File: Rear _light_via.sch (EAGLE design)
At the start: 9 parts

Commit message: via gerbers generated
via boards completed and gerbers generated
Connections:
- net N$4 renamed BRAKE_L
- net N$5 renamed DRIVE_R
- net N$6 renamed BRAKE_R
- net N$8 renamed DRIVE_L
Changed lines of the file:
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@@
 <?xml version="1.0" encoding="utf-8"?>
 <!DOCTYPE eagle SYSTEM "eagle.dtd">
-<eagle version="8.3.1">
+<eagle version="8.6.0">
 <drawing>
 <settings>
@@
 <wire x1="63.5" y1="27.94" x2="114.3" y2="27.94" width="0.1524" layer="91"/>
 <pinref part="L_DRIVE" gate="G$1" pin="V/SIG"/>
-</segment>
-</net>
-<net name="N$4" class="0">
+<label x="71.12" y="27.94" size="1.778" layer="95"/>
+</segment>
+</net>
+<net name="BRAKE_L" class="0">
 <segment>
 <pinref part="REAR" gate="G$1" pin="4"/>
@@
 <wire x1="101.6" y1="53.34" x2="102.87" y2="53.34" width="0.1524" layer="91"/>
 <wire x1="102.87" y1="53.34" x2="114.3" y2="53.34" width="0.1524" layer="91"/>
-</segment>
-</net>
-<net name="N$6" class="0">
+<label x="78.74" y="53.34" size="1.778" layer="95"/>
+</segment>
+</net>
+<net name="BRAKE_R" class="0">
 <segment>
 <pinref part="REAR" gate="G$1" pin="6"/>
@@
 <wire x1="101.6" y1="71.12" x2="102.87" y2="71.12" width="0.1524" layer="91"/>
 <wire x1="102.87" y1="71.12" x2="114.3" y2="71.12" width="0.1524" layer="91"/>
-</segment>
-</net>
-<net name="N$8" class="0">
+<label x="73.66" y="66.04" size="1.778" layer="95"/>
+</segment>
+</net>
+<net name="DRIVE_L" class="0">
 <segment>
 <pinref part="REAR" gate="G$1" pin="8"/>
@@
 <wire x1="86.36" y1="71.12" x2="86.36" y2="91.44" width="0.1524" layer="91"/>
 <wire x1="86.36" y1="91.44" x2="111.76" y2="91.44" width="0.1524" layer="91"/>
+<label x="73.66" y="71.12" size="1.778" layer="95"/>
 </segment>
 </net>
@@
 <pinref part="L_SIG" gate="G$1" pin="V/SIG"/>
 <wire x1="71.12" y1="48.26" x2="114.3" y2="48.26" width="0.1524" layer="91"/>
+<label x="76.2" y="48.26" size="1.778" layer="95"/>
 </segment>
 </net>
@@
 <pinref part="R_SIG" gate="G$1" pin="V/SIG"/>
 <wire x1="106.68" y1="66.04" x2="114.3" y2="66.04" width="0.1524" layer="91"/>
-</segment>
-</net>
-<net name="N$5" class="0">
+<label x="81.28" y="63.5" size="1.778" layer="95"/>
+</segment>
+</net>
+<net name="DRIVE_R" class="0">
 <segment>
 <pinref part="REAR" gate="G$1" pin="7"/>
@@
 <pinref part="L_DRIVE" gate="G$1" pin="G/LOW"/>
 <wire x1="58.42" y1="33.02" x2="114.3" y2="33.02" width="0.1524" layer="91"/>
+<label x="71.12" y="33.02" size="1.778" layer="95"/>
 </segment>
 </net>
@@
 <pinref part="T_DRIVE" gate="G$1" pin="V/SIG"/>
 <wire x1="66.04" y1="86.36" x2="111.76" y2="86.36" width="0.1524" layer="91"/>
-</segment>
-</net>
+<label x="71.12" y="86.36" size="1.778" layer="95"/>
+</segment>
+</net>

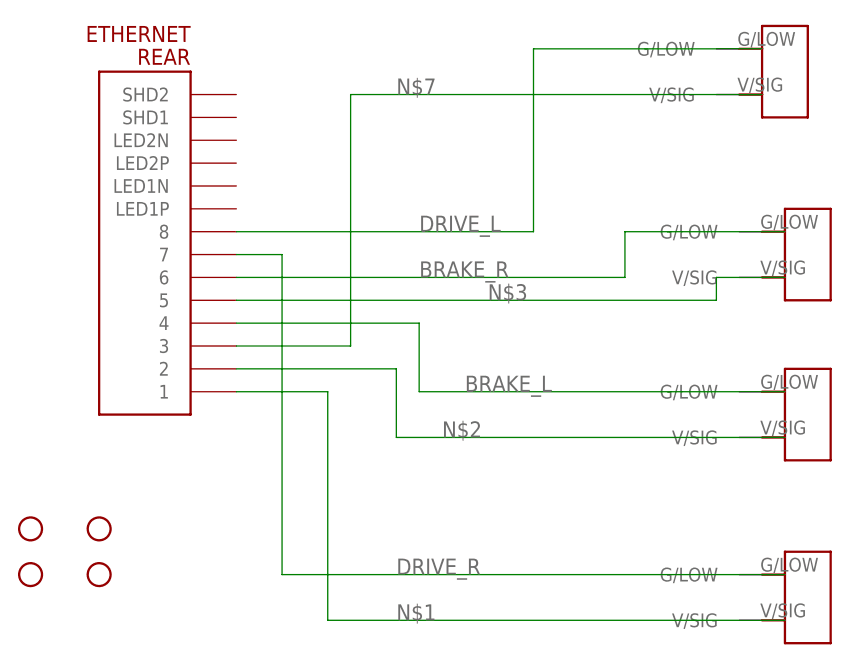
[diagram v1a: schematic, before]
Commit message: added reverse polairity protection
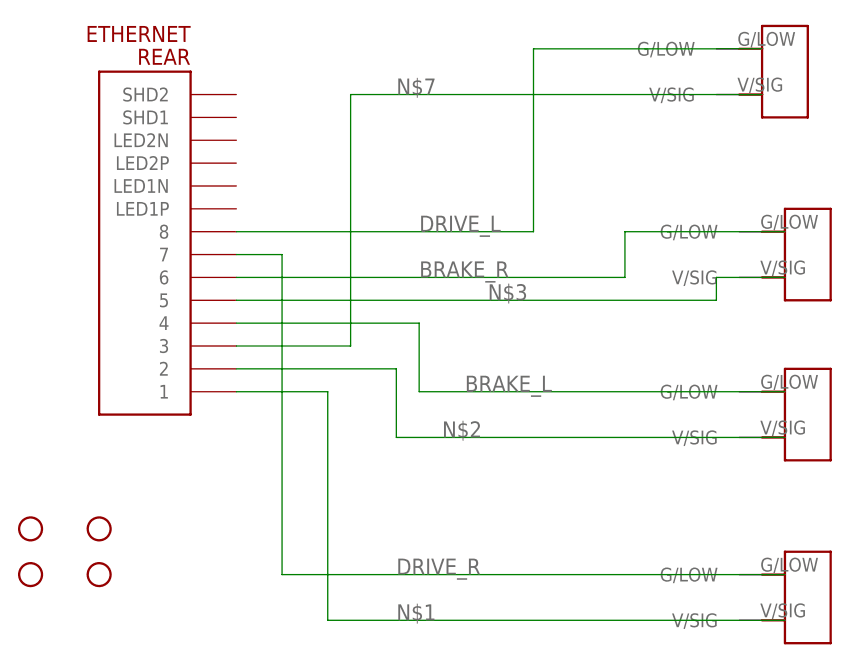
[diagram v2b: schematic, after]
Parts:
- renumbered L_DRIVE to U$4, L_SIG to U$3, R_SIG to U$2, T_DRIVE to U$1
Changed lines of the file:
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@@
 <?xml version="1.0" encoding="utf-8"?>
 <!DOCTYPE eagle SYSTEM "eagle.dtd">
-<eagle version="8.6.0">
+<eagle version="8.6.1">
 <drawing>
 <settings>
@@
 <parts>
 <part name="REAR" library="ETHERNET" deviceset="ETHERNET" device=""/>
-<part name="T_DRIVE" library="TE 2-pin connector" deviceset="2_PIN_TECONNECTOR" device=""/>
-<part name="R_SIG" library="TE 2-pin connector" deviceset="2_PIN_TECONNECTOR" device=""/>
-<part name="L_SIG" library="TE 2-pin connector" deviceset="2_PIN_TECONNECTOR" device=""/>
-<part name="L_DRIVE" library="TE 2-pin connector" deviceset="2_PIN_TECONNECTOR" device=""/>
 <part name="H1" library="SparkFun-Electromechanical" deviceset="STAND-OFF" device=""/>
 <part name="H2" library="SparkFun-Electromechanical" deviceset="STAND-OFF" device=""/>
 <part name="H3" library="SparkFun-Electromechanical" deviceset="STAND-OFF" device=""/>
 <part name="H4" library="SparkFun-Electromechanical" deviceset="STAND-OFF" device=""/>
+<part name="U$1" library="TE 2-pin connector" deviceset="2_PIN_TECONNECTOR" device=""/>
+<part name="U$2" library="TE 2-pin connector" deviceset="2_PIN_TECONNECTOR" device=""/>
+<part name="U$3" library="TE 2-pin connector" deviceset="2_PIN_TECONNECTOR" device=""/>
+<part name="U$4" library="TE 2-pin connector" deviceset="2_PIN_TECONNECTOR" device=""/>
 </parts>
 <sheets>
@@
 <instances>
 <instance part="REAR" gate="G$1" x="48.26" y="68.58" rot="R180"/>
-<instance part="T_DRIVE" gate="G$1" x="116.84" y="88.9"/>
-<instance part="R_SIG" gate="G$1" x="119.38" y="68.58"/>
-<instance part="L_SIG" gate="G$1" x="119.38" y="50.8"/>
-<instance part="L_DRIVE" gate="G$1" x="119.38" y="30.48"/>
 <instance part="H1" gate="G$1" x="30.48" y="38.1"/>
 <instance part="H2" gate="G$1" x="38.1" y="38.1"/>
 <instance part="H3" gate="G$1" x="30.48" y="33.02"/>
 <instance part="H4" gate="G$1" x="38.1" y="33.02"/>
+<instance part="U$1" gate="G$1" x="116.84" y="88.9"/>
+<instance part="U$2" gate="G$1" x="119.38" y="68.58"/>
+<instance part="U$3" gate="G$1" x="119.38" y="50.8"/>
+<instance part="U$4" gate="G$1" x="119.38" y="30.48"/>
 </instances>
 <busses>
@@
 <wire x1="63.5" y1="53.34" x2="63.5" y2="27.94" width="0.1524" layer="91"/>
 <wire x1="63.5" y1="27.94" x2="114.3" y2="27.94" width="0.1524" layer="91"/>
-<pinref part="L_DRIVE" gate="G$1" pin="V/SIG"/>
 <label x="71.12" y="27.94" size="1.778" layer="95"/>
+<pinref part="U$4" gate="G$1" pin="V/SIG"/>
 </segment>
 </net>
@@
 <wire x1="53.34" y1="60.96" x2="73.66" y2="60.96" width="0.1524" layer="91"/>
 <wire x1="73.66" y1="60.96" x2="73.66" y2="53.34" width="0.1524" layer="91"/>
-<wire x1="73.66" y1="53.34" x2="101.6" y2="53.34" width="0.1524" layer="91"/>
-<pinref part="L_SIG" gate="G$1" pin="G/LOW"/>
-<wire x1="101.6" y1="53.34" x2="102.87" y2="53.34" width="0.1524" layer="91"/>
-<wire x1="102.87" y1="53.34" x2="114.3" y2="53.34" width="0.1524" layer="91"/>
+<wire x1="73.66" y1="53.34" x2="114.3" y2="53.34" width="0.1524" layer="91"/>
 <label x="78.74" y="53.34" size="1.778" layer="95"/>
+<pinref part="U$3" gate="G$1" pin="G/LOW"/>
 </segment>
 </net>
@@
 <wire x1="53.34" y1="66.04" x2="96.52" y2="66.04" width="0.1524" layer="91"/>
 <wire x1="96.52" y1="66.04" x2="96.52" y2="71.12" width="0.1524" layer="91"/>
-<wire x1="96.52" y1="71.12" x2="101.6" y2="71.12" width="0.1524" layer="91"/>
-<pinref part="R_SIG" gate="G$1" pin="G/LOW"/>
-<wire x1="101.6" y1="71.12" x2="102.87" y2="71.12" width="0.1524" layer="91"/>
-<wire x1="102.87" y1="71.12" x2="114.3" y2="71.12" width="0.1524" layer="91"/>
+<wire x1="96.52" y1="71.12" x2="114.3" y2="71.12" width="0.1524" layer="91"/>
 <label x="73.66" y="66.04" size="1.778" layer="95"/>
+<pinref part="U$2" gate="G$1" pin="G/LOW"/>
 </segment>
 </net>
@@
 <pinref part="REAR" gate="G$1" pin="8"/>
 <wire x1="53.34" y1="71.12" x2="86.36" y2="71.12" width="0.1524" layer="91"/>
-<pinref part="T_DRIVE" gate="G$1" pin="G/LOW"/>
 <wire x1="86.36" y1="71.12" x2="86.36" y2="91.44" width="0.1524" layer="91"/>
 <wire x1="86.36" y1="91.44" x2="111.76" y2="91.44" width="0.1524" layer="91"/>
 <label x="73.66" y="71.12" size="1.778" layer="95"/>
+<pinref part="U$1" gate="G$1" pin="G/LOW"/>
 </segment>
 </net>
@@
 <wire x1="53.34" y1="55.88" x2="71.12" y2="55.88" width="0.1524" layer="91"/>
 <wire x1="71.12" y1="55.88" x2="71.12" y2="48.26" width="0.1524" layer="91"/>
-<pinref part="L_SIG" gate="G$1" pin="V/SIG"/>
 <wire x1="71.12" y1="48.26" x2="114.3" y2="48.26" width="0.1524" layer="91"/>
 <label x="76.2" y="48.26" size="1.778" layer="95"/>
+<pinref part="U$3" gate="G$1" pin="V/SIG"/>
 </segment>
 </net>
@@
 <wire x1="53.34" y1="63.5" x2="106.68" y2="63.5" width="0.1524" layer="91"/>
 <wire x1="106.68" y1="63.5" x2="106.68" y2="66.04" width="0.1524" layer="91"/>
-<pinref part="R_SIG" gate="G$1" pin="V/SIG"/>
 <wire x1="106.68" y1="66.04" x2="114.3" y2="66.04" width="0.1524" layer="91"/>
 <label x="81.28" y="63.5" size="1.778" layer="95"/>
+<pinref part="U$2" gate="G$1" pin="V/SIG"/>
 </segment>
 </net>
@@
 <wire x1="53.34" y1="68.58" x2="58.42" y2="68.58" width="0.1524" layer="91"/>
 <wire x1="58.42" y1="68.58" x2="58.42" y2="33.02" width="0.1524" layer="91"/>
-<pinref part="L_DRIVE" gate="G$1" pin="G/LOW"/>
 <wire x1="58.42" y1="33.02" x2="114.3" y2="33.02" width="0.1524" layer="91"/>
 <label x="71.12" y="33.02" size="1.778" layer="95"/>
+<pinref part="U$4" gate="G$1" pin="G/LOW"/>
 </segment>
 </net>
@@
 <wire x1="53.34" y1="58.42" x2="66.04" y2="58.42" width="0.1524" layer="91"/>
 <wire x1="66.04" y1="58.42" x2="66.04" y2="86.36" width="0.1524" layer="91"/>
-<pinref part="T_DRIVE" gate="G$1" pin="V/SIG"/>
 <wire x1="66.04" y1="86.36" x2="111.76" y2="86.36" width="0.1524" layer="91"/>
 <label x="71.12" y="86.36" size="1.778" layer="95"/>
-</segment>
-</net>
+<pinref part="U$1" gate="G$1" pin="V/SIG"/>
+</segment>
+</net>

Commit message: correct all routing errors
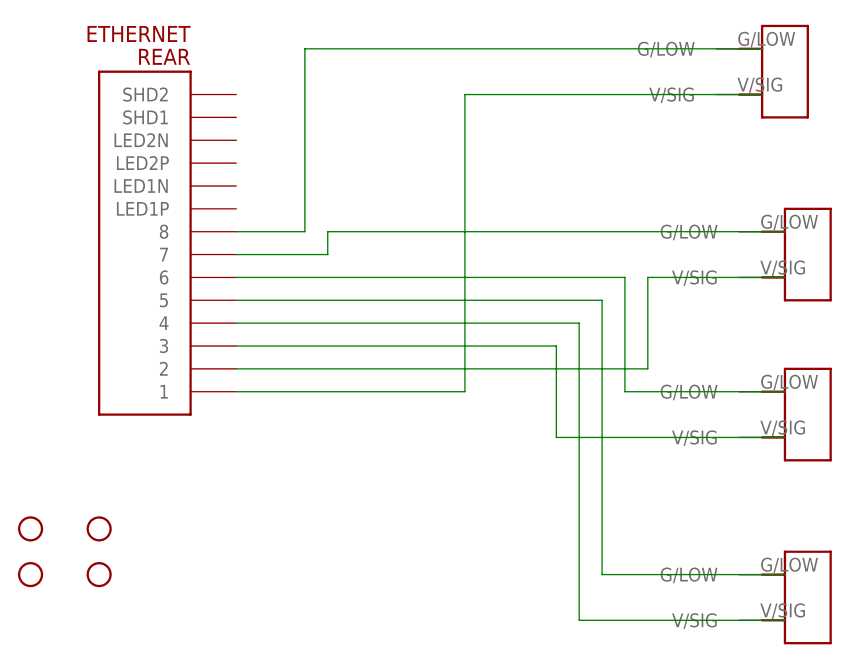
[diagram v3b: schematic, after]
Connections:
- net DRIVE_L renamed N$1
- removed net BRAKE_L: REAR.4, U$3.G/LOW
- removed net BRAKE_R: REAR.6, U$2.G/LOW
- removed net DRIVE_R: REAR.7, U$4.G/LOW
- removed net N$1 (its old number): REAR.1, U$4.V/SIG
- new net N$4: REAR.5, U$4.G/LOW
- new net N$5: REAR.4, U$4.V/SIG
- new net N$6: REAR.3, U$3.V/SIG
- new net N$8: REAR.1, U$1.V/SIG
- net N$2: now also REAR.7, U$2.G/LOW; no longer REAR.2, U$3.V/SIG
- net N$3: now also REAR.6, U$3.G/LOW; no longer REAR.5, U$2.V/SIG
- net N$7: now also REAR.2, U$2.V/SIG; no longer REAR.3, U$1.V/SIG
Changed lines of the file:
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@@
 <?xml version="1.0" encoding="utf-8"?>
 <!DOCTYPE eagle SYSTEM "eagle.dtd">
-<eagle version="8.6.1">
+<eagle version="9.0.0">
 <drawing>
 <settings>
@@
 <net name="N$1" class="0">
 <segment>
-<pinref part="REAR" gate="G$1" pin="1"/>
-<wire x1="53.34" y1="53.34" x2="63.5" y2="53.34" width="0.1524" layer="91"/>
-<wire x1="63.5" y1="53.34" x2="63.5" y2="27.94" width="0.1524" layer="91"/>
-<wire x1="63.5" y1="27.94" x2="114.3" y2="27.94" width="0.1524" layer="91"/>
-<label x="71.12" y="27.94" size="1.778" layer="95"/>
-<pinref part="U$4" gate="G$1" pin="V/SIG"/>
-</segment>
-</net>
-<net name="BRAKE_L" class="0">
-<segment>
-<pinref part="REAR" gate="G$1" pin="4"/>
-<wire x1="53.34" y1="60.96" x2="73.66" y2="60.96" width="0.1524" layer="91"/>
-<wire x1="73.66" y1="60.96" x2="73.66" y2="53.34" width="0.1524" layer="91"/>
-<wire x1="73.66" y1="53.34" x2="114.3" y2="53.34" width="0.1524" layer="91"/>
-<label x="78.74" y="53.34" size="1.778" layer="95"/>
-<pinref part="U$3" gate="G$1" pin="G/LOW"/>
-</segment>
-</net>
-<net name="BRAKE_R" class="0">
+<pinref part="REAR" gate="G$1" pin="8"/>
+<wire x1="53.34" y1="71.12" x2="60.96" y2="71.12" width="0.1524" layer="91"/>
+<wire x1="60.96" y1="71.12" x2="60.96" y2="91.44" width="0.1524" layer="91"/>
+<pinref part="U$1" gate="G$1" pin="G/LOW"/>
+<wire x1="60.96" y1="91.44" x2="111.76" y2="91.44" width="0.1524" layer="91"/>
+</segment>
+</net>
+<net name="N$2" class="0">
+<segment>
+<pinref part="U$2" gate="G$1" pin="G/LOW"/>
+<wire x1="114.3" y1="71.12" x2="63.5" y2="71.12" width="0.1524" layer="91"/>
+<wire x1="63.5" y1="71.12" x2="63.5" y2="68.58" width="0.1524" layer="91"/>
+<pinref part="REAR" gate="G$1" pin="7"/>
+<wire x1="63.5" y1="68.58" x2="53.34" y2="68.58" width="0.1524" layer="91"/>
+</segment>
+</net>
+<net name="N$3" class="0">
 <segment>
 <pinref part="REAR" gate="G$1" pin="6"/>
 <wire x1="53.34" y1="66.04" x2="96.52" y2="66.04" width="0.1524" layer="91"/>
-<wire x1="96.52" y1="66.04" x2="96.52" y2="71.12" width="0.1524" layer="91"/>
-<wire x1="96.52" y1="71.12" x2="114.3" y2="71.12" width="0.1524" layer="91"/>
-<label x="73.66" y="66.04" size="1.778" layer="95"/>
-<pinref part="U$2" gate="G$1" pin="G/LOW"/>
-</segment>
-</net>
-<net name="DRIVE_L" class="0">
-<segment>
-<pinref part="REAR" gate="G$1" pin="8"/>
-<wire x1="53.34" y1="71.12" x2="86.36" y2="71.12" width="0.1524" layer="91"/>
-<wire x1="86.36" y1="71.12" x2="86.36" y2="91.44" width="0.1524" layer="91"/>
-<wire x1="86.36" y1="91.44" x2="111.76" y2="91.44" width="0.1524" layer="91"/>
-<label x="73.66" y="71.12" size="1.778" layer="95"/>
-<pinref part="U$1" gate="G$1" pin="G/LOW"/>
-</segment>
-</net>
-<net name="N$2" class="0">
+<wire x1="96.52" y1="66.04" x2="96.52" y2="53.34" width="0.1524" layer="91"/>
+<pinref part="U$3" gate="G$1" pin="G/LOW"/>
+<wire x1="96.52" y1="53.34" x2="114.3" y2="53.34" width="0.1524" layer="91"/>
+</segment>
+</net>
+<net name="N$4" class="0">
+<segment>
+<pinref part="REAR" gate="G$1" pin="5"/>
+<wire x1="53.34" y1="63.5" x2="93.98" y2="63.5" width="0.1524" layer="91"/>
+<wire x1="93.98" y1="63.5" x2="93.98" y2="33.02" width="0.1524" layer="91"/>
+<pinref part="U$4" gate="G$1" pin="G/LOW"/>
+<wire x1="93.98" y1="33.02" x2="114.3" y2="33.02" width="0.1524" layer="91"/>
+</segment>
+</net>
+<net name="N$5" class="0">
+<segment>
+<pinref part="REAR" gate="G$1" pin="4"/>
+<wire x1="53.34" y1="60.96" x2="91.44" y2="60.96" width="0.1524" layer="91"/>
+<wire x1="91.44" y1="60.96" x2="91.44" y2="27.94" width="0.1524" layer="91"/>
+<pinref part="U$4" gate="G$1" pin="V/SIG"/>
+<wire x1="114.3" y1="27.94" x2="91.44" y2="27.94" width="0.1524" layer="91"/>
+</segment>
+</net>
+<net name="N$6" class="0">
+<segment>
+<pinref part="REAR" gate="G$1" pin="3"/>
+<wire x1="53.34" y1="58.42" x2="88.9" y2="58.42" width="0.1524" layer="91"/>
+<wire x1="88.9" y1="58.42" x2="88.9" y2="48.26" width="0.1524" layer="91"/>
+<pinref part="U$3" gate="G$1" pin="V/SIG"/>
+<wire x1="88.9" y1="48.26" x2="114.3" y2="48.26" width="0.1524" layer="91"/>
+</segment>
+</net>
+<net name="N$7" class="0">
 <segment>
 <pinref part="REAR" gate="G$1" pin="2"/>
-<wire x1="53.34" y1="55.88" x2="71.12" y2="55.88" width="0.1524" layer="91"/>
-<wire x1="71.12" y1="55.88" x2="71.12" y2="48.26" width="0.1524" layer="91"/>
-<wire x1="71.12" y1="48.26" x2="114.3" y2="48.26" width="0.1524" layer="91"/>
-<label x="76.2" y="48.26" size="1.778" layer="95"/>
-<pinref part="U$3" gate="G$1" pin="V/SIG"/>
-</segment>
-</net>
-<net name="N$3" class="0">
-<segment>
-<pinref part="REAR" gate="G$1" pin="5"/>
-<wire x1="53.34" y1="63.5" x2="106.68" y2="63.5" width="0.1524" layer="91"/>
-<wire x1="106.68" y1="63.5" x2="106.68" y2="66.04" width="0.1524" layer="91"/>
-<wire x1="106.68" y1="66.04" x2="114.3" y2="66.04" width="0.1524" layer="91"/>
-<label x="81.28" y="63.5" size="1.778" layer="95"/>
+<wire x1="53.34" y1="55.88" x2="99.06" y2="55.88" width="0.1524" layer="91"/>
+<wire x1="99.06" y1="55.88" x2="99.06" y2="66.04" width="0.1524" layer="91"/>
 <pinref part="U$2" gate="G$1" pin="V/SIG"/>
-</segment>
-</net>
-<net name="DRIVE_R" class="0">
-<segment>
-<pinref part="REAR" gate="G$1" pin="7"/>
-<wire x1="53.34" y1="68.58" x2="58.42" y2="68.58" width="0.1524" layer="91"/>
-<wire x1="58.42" y1="68.58" x2="58.42" y2="33.02" width="0.1524" layer="91"/>
-<wire x1="58.42" y1="33.02" x2="114.3" y2="33.02" width="0.1524" layer="91"/>
-<label x="71.12" y="33.02" size="1.778" layer="95"/>
-<pinref part="U$4" gate="G$1" pin="G/LOW"/>
-</segment>
-</net>
-<net name="N$7" class="0">
-<segment>
-<pinref part="REAR" gate="G$1" pin="3"/>
-<wire x1="53.34" y1="58.42" x2="66.04" y2="58.42" width="0.1524" layer="91"/>
-<wire x1="66.04" y1="58.42" x2="66.04" y2="86.36" width="0.1524" layer="91"/>
-<wire x1="66.04" y1="86.36" x2="111.76" y2="86.36" width="0.1524" layer="91"/>
-<label x="71.12" y="86.36" size="1.778" layer="95"/>
+<wire x1="99.06" y1="66.04" x2="114.3" y2="66.04" width="0.1524" layer="91"/>
+</segment>
+</net>
+<net name="N$8" class="0">
+<segment>
+<pinref part="REAR" gate="G$1" pin="1"/>
+<wire x1="53.34" y1="53.34" x2="78.74" y2="53.34" width="0.1524" layer="91"/>
+<wire x1="78.74" y1="53.34" x2="78.74" y2="86.36" width="0.1524" layer="91"/>
 <pinref part="U$1" gate="G$1" pin="V/SIG"/>
-</segment>
-</net>
+<wire x1="78.74" y1="86.36" x2="111.76" y2="86.36" width="0.1524" layer="91"/>
+</segment>
+</net>
